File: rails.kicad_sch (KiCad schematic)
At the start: 85 parts, among them U13 LM61460AASQRJRRQ1, U4 HUSB238_002DD, U5 TPS259474ARPWR, U6 LM61460AASQRJRRQ1

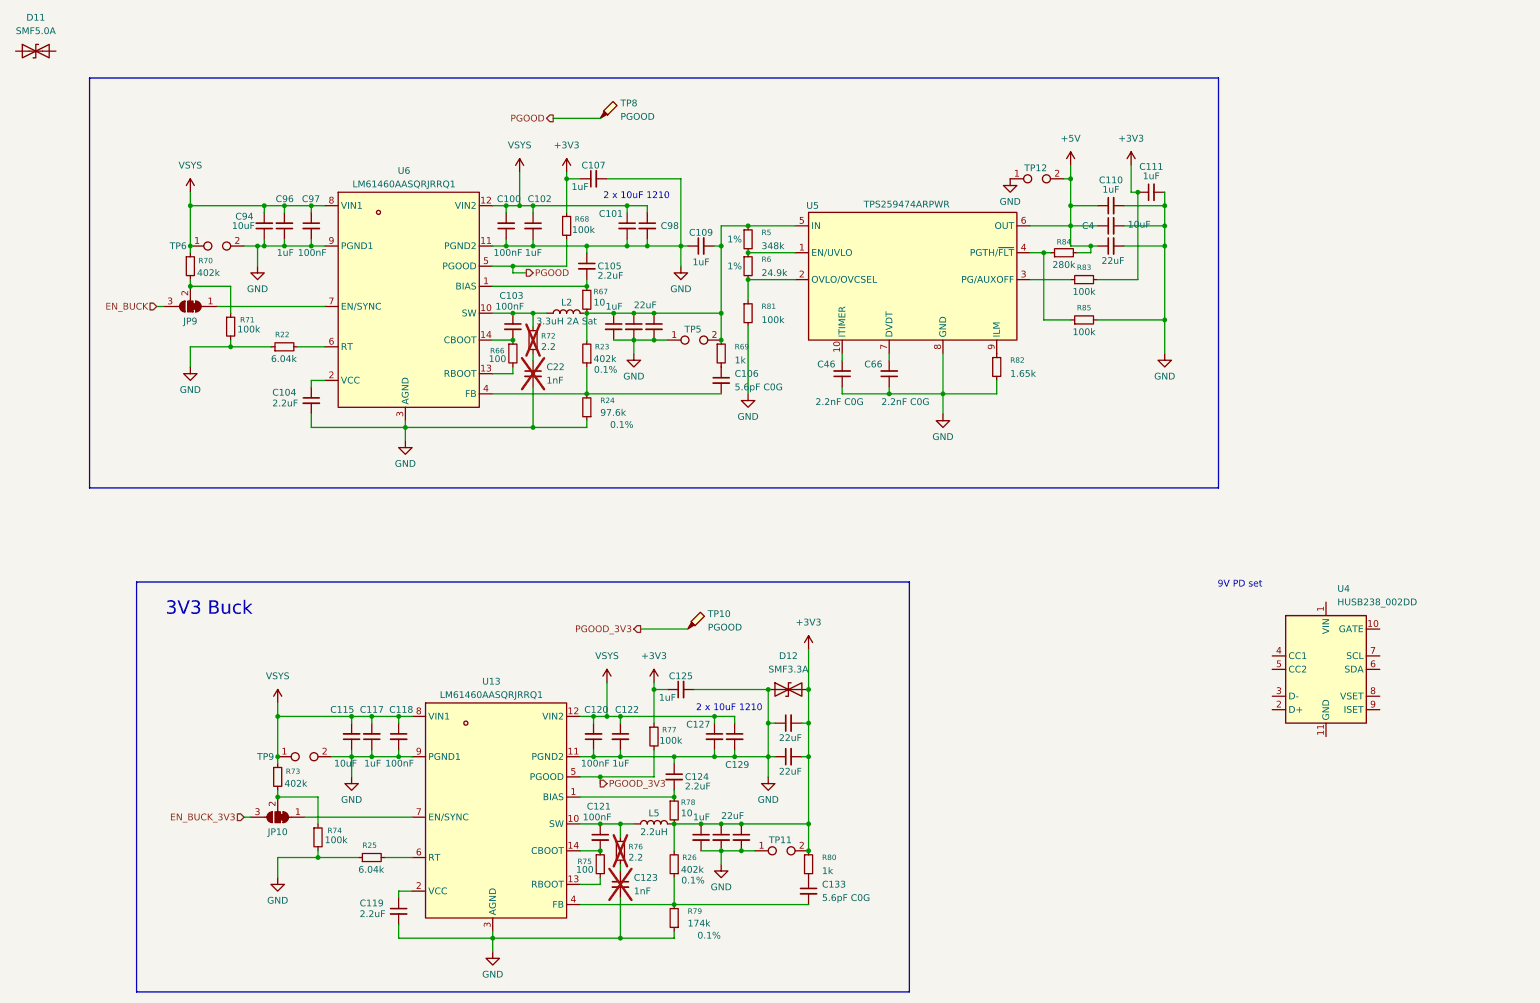
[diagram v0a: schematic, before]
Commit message: Reworking power rails, adding antenna detection, and organization
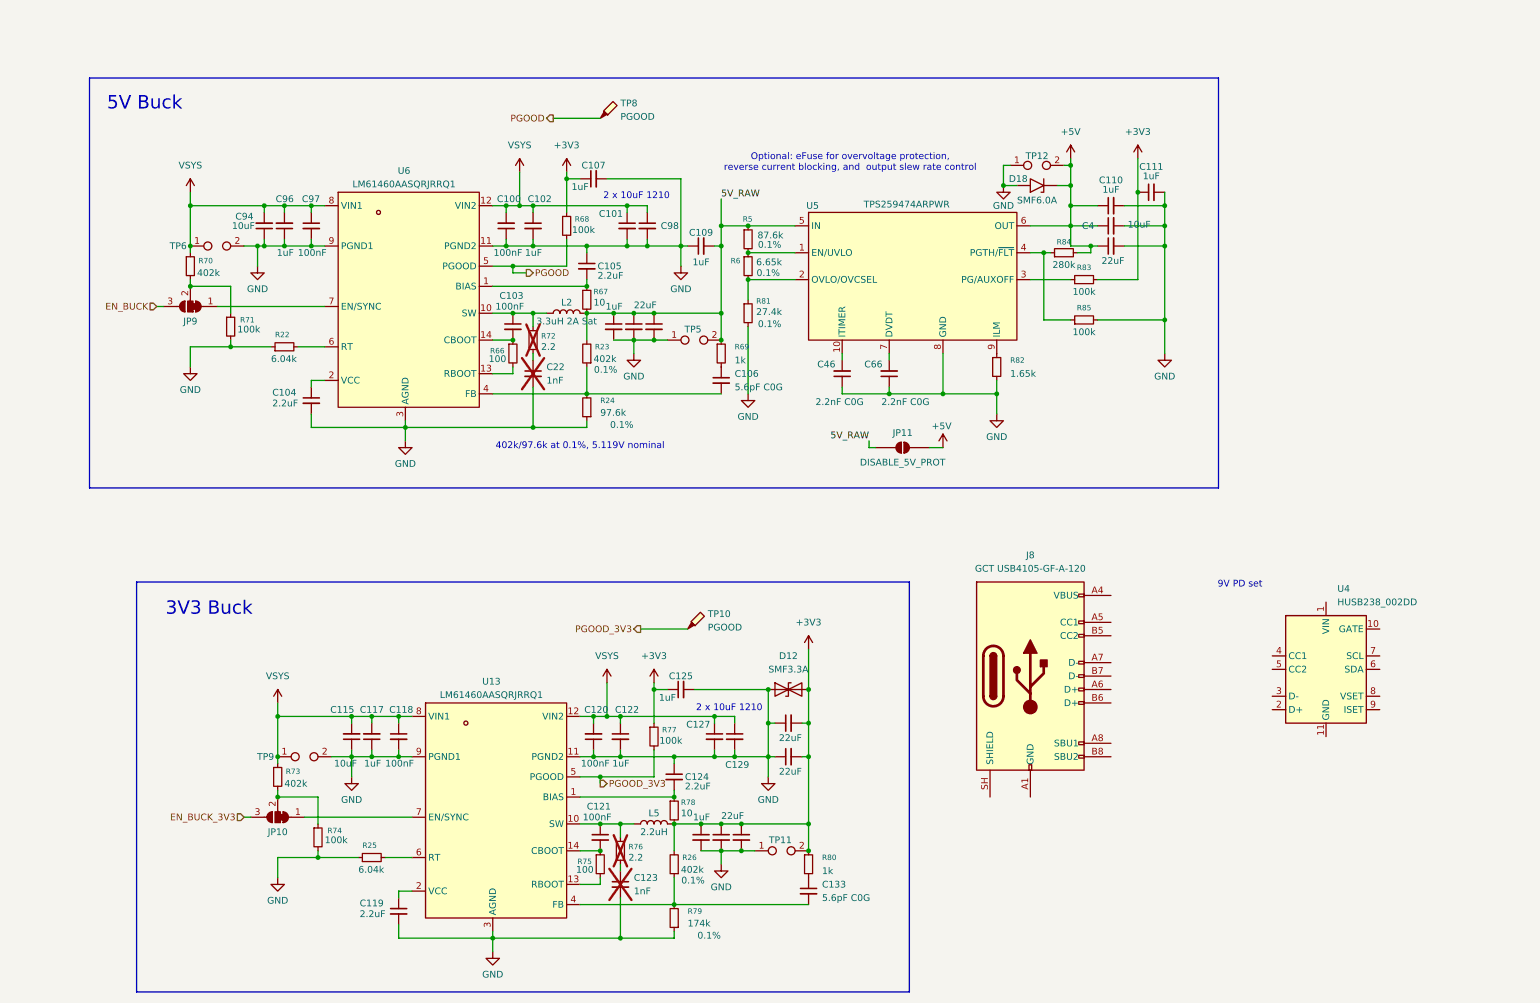
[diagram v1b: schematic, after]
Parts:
- removed D11: SMF5.0A, symbol Device:D_TVS
- added D18: SMF6.0A, Diode_SMD:D_SOD-123, symbol Diode:SMF6V0A
- added J8: GCT USB4105-GF-A-120, Connector_USB:USB_C_Receptacle_GCT_USB4105-xx-A_16P_TopMnt_Horizontal, symbol Connector:USB_C_Receptacle_USB2.0_16P
- added JP11: DISABLE_5V_PROT, symbol Jumper:SolderJumper_2_Open
- R5: value 348k -> 87.6k; Tolerance 1% -> 0.1%
- R6: value 24.9k -> 6.65k; Tolerance 1% -> 0.1%
- R81: value 100k -> 27.4k; Tolerance (none) -> 0.1%
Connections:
- net +5V: now also D18.1 (A1), JP11.2 (B)
- net GND: now also D18.2 (A2)
- net 5V_RAW: now reaches C109.2, C21.1, C23.1, C92.1, L2.2, R23.2, R5.1, R67.2, R69.1, TP5.2, U5.5 (IN)
- net 5V_RAW: now also JP11.1 (A)
- new net: J8.A1 (GND), J8.A12 (GND), J8.B1 (GND), J8.B12 (GND)
- new net: J8.A4 (VBUS), J8.A9 (VBUS), J8.B4 (VBUS), J8.B9 (VBUS)
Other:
- note added: "402k/97.6k at 0.1%, 5.119V nominal"
- note added: "5V Buck"
- note added: "Optional: eFuse for overvoltage protection, reverse current blocking, and output slew rate control"
- moved on the sheet: TP12

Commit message: push to work on laptop
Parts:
- removed J8: GCT USB4105-GF-A-120, Connector_USB:USB_C_Receptacle_GCT_USB4105-xx-A_16P_TopMnt_Horizontal, symbol Connector:USB_C_Receptacle_USB2.0_16P
- removed U4: HUSB238_002DD, Package_DFN_QFN:WDFN-10-1EP_3x3mm_P0.5mm_EP1.8x2.5mm, symbol Interface_USB:HUSB238_xxxDD
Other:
- note removed: "9V PD set"

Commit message: usb-org
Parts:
- added C137, C138, C139, C140, C141: 22uF, Capacitor_SMD:C_1210_3225Metric, symbol Device:C_Small
- L2: LCSC Part C3002593 -> (none)
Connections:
- net +5V: now also C137.1, C138.1, C139.1, C140.1, C141.1
- net GND: now also C137.2, C138.2, C139.2, C140.2, C141.2
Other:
- note added: "5 x 22uF"
- moved on the sheet: C100, C101, C102, C103, C104, C105, C106, C107, C109, C110, C111, C115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

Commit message: push to work on laptop2
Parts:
- removed D12: SMF3.3A, symbol Device:D_TVS
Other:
- company: (none) -> Ryan Di Lorenzo
- title: (none) -> Power Regulators
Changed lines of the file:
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@@
 	(paper "A4")
 	(title_block
+		(title "Power Regulators")
 		(date "2026-05-14")
+		(company "Ryan Di Lorenzo")
 	)
 	(rectangle
@@
 	)
 	(junction
-		(at 144.78 135.89)
-		(diameter 0)
-		(color 0 0 0 0)
-	)
-	(junction
 		(at 127 64.77)
 		(diameter 0)
@@
 	)
 	(junction
-		(at 152.4 135.89)
-		(diameter 0)
-		(color 0 0 0 0)
-	)
-	(junction
 		(at 135.89 161.29)
 		(diameter 0)
@@
 	(wire
 		(pts
-			(xy 152.4 135.89) (xy 152.4 142.24)
+			(xy 152.4 128.27) (xy 152.4 142.24)
 		)
 		(stroke
@@
 	(wire
 		(pts
-			(xy 152.4 128.27) (xy 152.4 135.89)
-		)
-		(stroke
-			(width 0)
-			(type default)
-		)
-	)
-	(wire
-		(pts
 			(xy 85.09 64.77) (xy 90.17 64.77)
 		)
@@
 					(unit 1)
 				)
-			)
-		)
-	)
-	(symbol
-		(lib_id "Device:D_TVS")
-		(at 148.59 135.89 0)
-		(unit 1)
-		(body_style 1)
-		(exclude_from_sim no)
-		(in_bom yes)
-		(on_board yes)
-		(in_pos_files yes)
-		(dnp no)
-		(fields_autoplaced yes)
-		(property "Reference" "D12"
-			(at 148.59 129.54 0)
-			(show_name no)
-			(do_not_autoplace no)
-			(effects
-				(font
-					(size 1.27 1.27)
-				)
-			)
-		)
-		(property "Value" "SMF3.3A"
-			(at 148.59 132.08 0)
-			(show_name no)
-			(do_not_autoplace no)
-			(effects
-				(font
-					(size 1.27 1.27)
-				)
-			)
-		)
-		(property "Footprint" ""
-			(at 148.59 135.89 0)
-			(hide yes)
-			(show_name no)
-			(do_not_autoplace no)
-			(effects
-				(font
-					(size 1.27 1.27)
-				)
-			)
-		)
-		(property "Datasheet" ""
-			(at 148.59 135.89 0)
-			(hide yes)
-			(show_name no)
-			(do_not_autoplace no)
-			(effects
-				(font
-					(size 1.27 1.27)
-				)
-			)
-		)
-		(property "Description" "Bidirectional transient-voltage-suppression diode"
-			(at 148.59 135.89 0)
-			(hide yes)
-			(show_name no)
-			(do_not_autoplace no)
-			(effects
-				(font
-					(size 1.27 1.27)
-				)
-			)
-		)
-		(property "LCSC Part" ""
-			(at 148.59 135.89 0)
-			(hide yes)
-			(show_name no)
-			(do_not_autoplace no)
-			(effects
-				(font
-					(size 1.27 1.27)
-				)
-			)
-		)
-		(property "Voltage Rating" ""
-			(at 148.59 135.89 0)
-			(show_name no)
-			(do_not_autoplace no)
-			(effects
-				(font
-					(size 1.27 1.27)
-				)
-			)
-		)
-		(property "Tolerance" ""
-			(at 148.59 135.89 0)
-			(show_name no)
-			(do_not_autoplace no)
-			(effects
-				(font
-					(size 1.27 1.27)
-				)
-			)
-		)
-		(pin "2"
-		)
-		(pin "1"
-		)
-		(instances
-			(project "parsnip"
-				(path "/d6234e85-43d0-45a0-a015-7fe7290a693b"
-					(reference "D12")
-					(unit 1)
-				)

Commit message: push for review, minor changes
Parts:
- removed JP9: SolderJumper_3_Bridged12, Jumper:SolderJumper-3_P1.3mm_Bridged12_RoundedPad1.0x1.5mm_NumberLabels, symbol Jumper:SolderJumper_3_Bridged12
- added Q11: 2N7002, Package_TO_SOT_SMD:SOT-23, symbol Transistor_FET:2N7002
- added R84: 100, symbol Device:R_Small
- added R87: 100k, symbol Device:R_Small
- added TP7: EN_3V3, symbol Connector:TestPoint_Probe
- renumbered C115 to C108, C117 to C109, C118 to C110, C119 to C111, C94 to C112, C96 to C113, C97 to C114, C104 to C115, C120 to C116, C121 to C117, C122 to C118, C123 to C119, C100 to C120, C124 to C121, C103 to C122, C125 to C123, C102 to C124, C22 to C125, C105 to C131, C107 to C132, C92 to C133, C132 to C135, C101 to C136, C21 to C137, C133 to C138, C98 to C139, C23 to C140, C109 to C141, C106 to C142, C46 to C143, C66 to C144, C137 to C145, C138 to C146, C110 to C147, C4 to C148, C24 to C149, C139 to C150, C140 to C151, C111 to C152, C141 to C153, D18 to D16, JP10 to JP15, JP11 to JP16, L5 to L4, L2 to L5, R68 to R100, R67 to R101, R23 to R102, R24 to R103, R80 to R104, R69 to R105, R5 to R106, R6 to R107, R81 to R108, R82 to R109, R84 to R110, R83 to R111, R85 to R112, R73 to R85, R74 to R86, R70 to R88, R71 to R89, R25 to R90, R22 to R91, R75 to R92, R76 to R93, R77 to R94, R78 to R95, R26 to R96, R79 to R97, R66 to R98, R72 to R99, TP8 to TP11, TP11 to TP12, TP5 to TP13, TP12 to TP14, TP9 to TP8, TP6 to TP9, U13 to U12, U6 to U13, U5 to U14
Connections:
- net GND: now also Q11.2 (S), R87.2
- net at R88.2, R89.1: now also U13.7 (EN/SYNC), Q11.3 (D)
- net EN_BUCK_3V3: no longer names the net of JP15.3 (B)
- net EN_BUCK_3V3: now also TP7.1
- net PGOOD renamed PGOOD_5V
- new net: Q11.1 (G), R84.2, R87.1
- new net EN_BUCK_5V: R84.1
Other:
- moved on the sheet: R89

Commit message: journal update!
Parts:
- added C158, C159, C162: 1uF, Capacitor_SMD:C_0402_1005Metric, symbol Device:C_Small
- added C160, C161: 1nF, Capacitor_SMD:C_0402_1005Metric, symbol Device:C_Small
- added C167, C168, C171: 22uF, Capacitor_SMD:C_1206_3216Metric, symbol Device:C_Small
- added D19: BAT54A, Package_TO_SOT_SMD:SOT-23, symbol Diode:BAT54A
- added D3: BAT54W, Package_TO_SOT_SMD:SOT-323_SC-70, symbol Diode:BAT54W
- added R119: 10k, symbol Device:R_Small
- added U15: SN74LVC1G74, Package_SON:X2SON-8_1.4x1mm_P0.35mm, symbol 74xGxx:74LVC2G74
- added Y2: SX1M4.000M10F30TNN, Oscillator:Oscillator_SMD_SiT_PQFN-4Pin_2.0x1.6mm, symbol Oscillator:SiT8008xx-7x-xxS
- C110, C114, C116, C120: Capacitor Rating (none) -> X7R; LCSC Part (none) -> C5142567
- C117, C122: Capacitor Rating (none) -> X7R; LCSC Part (none) -> C5142567; Voltage Rating 25V -> 50V
- C119, C125: value 1nF -> 220pF
- L4: footprint (none) -> Inductor_SMD:L_Sunlord_MWSA1005S; LCSC Part C3002593 -> C48391620
- L5: value 3.3uH 2A Sat -> 3.3uH 11A Sat; footprint (none) -> Inductor_SMD:L_APV_APH1040; LCSC Part (none) -> C439020
- R100, R94: value 100k -> 10k
- R103: value 97.6k -> 101k
- R106: value 87.6k -> 86.6k
- R107: value 6.65k -> 3.92k
- R109: value 1.65k -> 556; footprint (none) -> Resistor_SMD:R_0402_1005Metric_Pad0.72x0.64mm_HandSolder; Tolerance (none) -> 1%
- R93, R99: value 2.2 -> 2.2 0.25W
- TP13: value PRE_5V -> 5V_RAW
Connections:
- net +3V3: now also C159.1, C162.1, C167.2, R119.1, U15.6 (~{CLR}), U15.7 (~{PRE}), U15.8 (VCC), Y2.4 (VDD)
- net +5V: now also C168.1, C171.1
- net 5V_RAW: now also C158.2
- net GND: now also C158.1, C159.2, C162.2, C167.1, C168.2, C171.2, U15.4 (GND), Y2.2 (GND)
- net PGOOD_3V3: now also D19.2
- net PGOOD_5V: now also D3.3 (K)
- net PGOOD_EFUSE: now reaches R111.1, U14.3 (PG/AUXOFF)
- net SYNC_2: now reaches JP15.1 (A), U12.7 (EN/SYNC)
- net SYNC_2: now also C161.1
- net SYNC_1: now reaches Q11.3 (D), R88.2, R89.1, U13.7 (EN/SYNC)
- net SYNC_1: now also C160.1
- new net: D19.3, D3.1 (A), R119.2, Y2.1 (~{ST})
- new net: U15.1 (C), Y2.3 (OUT)
- new net: C160.2, U15.2 (D), U15.3 (~{Q})
- new net: C161.2, U15.5 (Q)
- new net EN_CLOCK: D19.1
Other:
- note added: "402k/100k at 0.1%, 5.020V nominal"
- note added: "4MHz / 2 = 2MHz each buck"
- note added: "Optional: Buck's VIN 180 degrees out of phase with eachother for less EMI"
- note removed: "402k/97.6k at 0.1%, 5.119V nominal"
- moved on the sheet: C141, C147, C148, C152, R110, R111, R93, R99

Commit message: pcb layout!
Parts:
- C122: renamed from C108; footprint Capacitor_SMD:C_1210_3225Metric -> Capacitor_SMD:C_1206_3216Metric; LCSC Part C7472976 -> C49326770
- C124: renamed from C110; LCSC Part C5142567 -> C5272680
- C125: renamed from C111; LCSC Part (none) -> C7432769
- C126: renamed from C112; footprint Capacitor_SMD:C_1210_3225Metric -> Capacitor_SMD:C_1206_3216Metric; LCSC Part C7472976 -> C49326770
- C128: renamed from C114; LCSC Part C5142567 -> C5272680
- C129: renamed from C115; LCSC Part (none) -> C7432769
- C130: renamed from C116; LCSC Part C5142567 -> C5272680
- C131: renamed from C117; LCSC Part C5142567 -> C5272680
- C132: renamed from C118; footprint Capacitor_SMD:C_0603_1608Metric -> Capacitor_SMD:C_0402_1005Metric; LCSC Part (none) -> C53426846
- C134: renamed from C120; LCSC Part C5142567 -> C5272680
- C135: renamed from C121; LCSC Part (none) -> C7432769
- C136: renamed from C122; LCSC Part C5142567 -> C5272680
- C137: renamed from C123; LCSC Part (none) -> C7472948
- C138: renamed from C124; footprint Capacitor_SMD:C_0603_1608Metric -> Capacitor_SMD:C_0402_1005Metric; LCSC Part (none) -> C53426846
- C140: renamed from C126; LCSC Part (none) -> C53426846
- C141: renamed from C127; footprint Capacitor_SMD:C_1210_3225Metric -> Capacitor_SMD:C_1206_3216Metric; LCSC Part C7472976 -> C49326770
- C142: renamed from C128; footprint (none) -> Capacitor_SMD:C_0603_1608Metric; LCSC Part (none) -> C22392391
- C143: renamed from C129; footprint Capacitor_SMD:C_1210_3225Metric -> Capacitor_SMD:C_1206_3216Metric; LCSC Part C7472976 -> C49326770
- C144: renamed from C130; LCSC Part (none) -> C48579675
- C145: renamed from C131; LCSC Part (none) -> C7432769
- C146: renamed from C132; LCSC Part (none) -> C7472948
- C147: renamed from C133; LCSC Part (none) -> C53426846
- C148: renamed from C167; LCSC Part (none) -> C48579675
- C149: renamed from C134; LCSC Part (none) -> C48579675
- C150: renamed from C135; LCSC Part (none) -> C48579675
- C151: renamed from C136; footprint Capacitor_SMD:C_1210_3225Metric -> Capacitor_SMD:C_1206_3216Metric; LCSC Part C7472976 -> C49326770
- C152: renamed from C137; footprint (none) -> Capacitor_SMD:C_0603_1608Metric; LCSC Part (none) -> C22392391
- C153: renamed from C138; value 5.6pF C0G -> 5.6pF; Capacitor Rating (none) -> C0G; LCSC Part (none) -> C525219
- C154: renamed from C139; footprint Capacitor_SMD:C_1210_3225Metric -> Capacitor_SMD:C_1206_3216Metric; LCSC Part C7472976 -> C49326770
- C155: renamed from C140; LCSC Part (none) -> C48579675
- C156: renamed from C141; LCSC Part (none) -> C53426846
- C157: renamed from C158; LCSC Part (none) -> C53426846
- C158: renamed from C142; value 5.6pF C0G -> 5.6pF; Capacitor Rating (none) -> C0G; LCSC Part (none) -> C525219
- C159: renamed from C160; LCSC Part (none) -> C54916656
- C160: renamed from C161; LCSC Part (none) -> C54916656
- C161: renamed from C143; value 2.2nF C0G -> 2.2nF; Capacitor Rating (none) -> C0G; LCSC Part (none) -> C2987940
- C162: renamed from C144; value 2.2nF C0G -> 2.2nF; Capacitor Rating (none) -> C0G; LCSC Part (none) -> C2987940
- C163: renamed from C162; LCSC Part (none) -> C53426846
- C164: renamed from C159; LCSC Part (none) -> C53426846
- C165: renamed from C145; footprint Capacitor_SMD:C_1210_3225Metric -> Capacitor_SMD:C_1206_3216Metric; LCSC Part C2918511 -> C48579675
- C166: renamed from C146; footprint Capacitor_SMD:C_1210_3225Metric -> Capacitor_SMD:C_1206_3216Metric; LCSC Part C2918511 -> C48579675
- C167: renamed from C147; LCSC Part (none) -> C53426846
- C168: renamed from C148; footprint Capacitor_SMD:C_0805_2012Metric -> Capacitor_SMD:C_0603_1608Metric; LCSC Part (none) -> C22392391
- C169: renamed from C168; LCSC Part (none) -> C48579675
- C170: renamed from C149; LCSC Part (none) -> C48579675
- C171: LCSC Part (none) -> C48579675
- C172: renamed from C150; footprint Capacitor_SMD:C_1210_3225Metric -> Capacitor_SMD:C_1206_3216Metric; LCSC Part C2918511 -> C48579675
- C173: renamed from C151; footprint Capacitor_SMD:C_1210_3225Metric -> Capacitor_SMD:C_1206_3216Metric; LCSC Part C2918511 -> C48579675
- C174: renamed from C152; LCSC Part (none) -> C53426846
- C175: renamed from C153; footprint Capacitor_SMD:C_1210_3225Metric -> Capacitor_SMD:C_1206_3216Metric; LCSC Part C2918511 -> C48579675
- D20: renamed from D16; footprint Diode_SMD:D_SOD-123 -> Diode_SMD:D_SOD-123F; LCSC Part (none) -> C2758490
- D22: renamed from D3; LCSC Part (none) -> C5186013
- JP17: renamed from JP16; footprint (none) -> Jumper:SolderJumper-2_P1.3mm_Open_RoundedPad1.0x1.5mm
- L4: footprint Inductor_SMD:L_Sunlord_MWSA1005S -> Inductor_SMD:L_Sunlord_MWSA1003S
- Q15: renamed from Q11; LCSC Part (none) -> C5331134
- R103: renamed from R84; footprint (none) -> Resistor_SMD:R_0402_1005Metric; LCSC Part (none) -> C55174701
- R104: renamed from R85; footprint (none) -> Resistor_SMD:R_0603_1608Metric; LCSC Part (none) -> C29269954
- R105: renamed from R86; footprint (none) -> Resistor_SMD:R_0402_1005Metric; LCSC Part (none) -> C2984406
- R106: renamed from R87; footprint (none) -> Resistor_SMD:R_0402_1005Metric; LCSC Part (none) -> C2984406
- R107: renamed from R88; footprint (none) -> Resistor_SMD:R_0603_1608Metric; LCSC Part (none) -> C29269954
- R108: renamed from R89; footprint (none) -> Resistor_SMD:R_0402_1005Metric; LCSC Part (none) -> C2984406
- R109: renamed from R90; LCSC Part (none) -> C852895
- R110: renamed from R91; LCSC Part (none) -> C852895
- R111: renamed from R92; LCSC Part (none) -> C55174701
- R112: renamed from R93; value 2.2 0.25W -> 2.2; footprint Resistor_SMD:R_0402_1005Metric_Pad0.72x0.64mm_HandSolder -> Resistor_SMD:R_0805_2012Metric; LCSC Part (none) -> C5925229; Power Rating (none) -> 250mW
- R113: renamed from R94; footprint (none) -> Resistor_SMD:R_0402_1005Metric; LCSC Part (none) -> C2902636
- R114: renamed from R95; LCSC Part (none) -> C1883546
- R115: renamed from R96; footprint Resistor_SMD:R_0402_1005Metric -> Resistor_SMD:R_0603_1608Metric; LCSC Part (none) -> C29269954
- R116: renamed from R97; LCSC Part (none) -> C852565
- R117: renamed from R98; LCSC Part (none) -> C55174701
- R118: renamed from R99; value 2.2 0.25W -> 2.2; footprint Resistor_SMD:R_0402_1005Metric_Pad0.72x0.64mm_HandSolder -> Resistor_SMD:R_0805_2012Metric; LCSC Part (none) -> C5925229; Power Rating (none) -> 250mW
- R119: renamed from R100; footprint (none) -> Resistor_SMD:R_0402_1005Metric; LCSC Part (none) -> C2902636
- R120: renamed from R101; LCSC Part (none) -> C1883546
- R121: renamed from R102; footprint Resistor_SMD:R_0402_1005Metric -> Resistor_SMD:R_0603_1608Metric; LCSC Part (none) -> C29269954
- R122: renamed from R103; footprint Resistor_SMD:R_0402_1005Metric_Pad0.72x0.64mm_HandSolder -> Resistor_SMD:R_0805_2012Metric_Pad1.20x1.40mm_HandSolder; LCSC Part (none) -> C7302896
- R123: renamed from R104; LCSC Part (none) -> C48533754
- R124: renamed from R105; LCSC Part (none) -> C48533754
- R125: renamed from R106; footprint (none) -> Resistor_SMD:R_0402_1005Metric; LCSC Part (none) -> C852935
- R126: renamed from R107; footprint (none) -> Resistor_SMD:R_0402_1005Metric; LCSC Part (none) -> C2692963
- R127: renamed from R108; footprint (none) -> Resistor_SMD:R_0402_1005Metric; LCSC Part (none) -> C852679
- R128: renamed from R109; value 556 -> 750
- R129: renamed from R110; footprint (none) -> Resistor_SMD:R_0603_1608Metric; LCSC Part (none) -> C861797
- R130: renamed from R112; footprint (none) -> Resistor_SMD:R_0402_1005Metric; LCSC Part (none) -> C2984406
- R131: renamed from R111; footprint (none) -> Resistor_SMD:R_0402_1005Metric; LCSC Part (none) -> C2984406
- R132: renamed from R119; footprint (none) -> Resistor_SMD:R_0402_1005Metric; LCSC Part (none) -> C2902636
- TP7: footprint (none) -> TestPoint:TestPoint_Pad_D1.5mm
- renumbered C109 to C123, C113 to C127, C119 to C133, C125 to C139, D19 to D21, JP15 to JP16, U12 to U13, U13 to U14, U14 to U15, U15 to U16
